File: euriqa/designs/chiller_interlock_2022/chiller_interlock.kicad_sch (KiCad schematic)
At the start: 0 parts

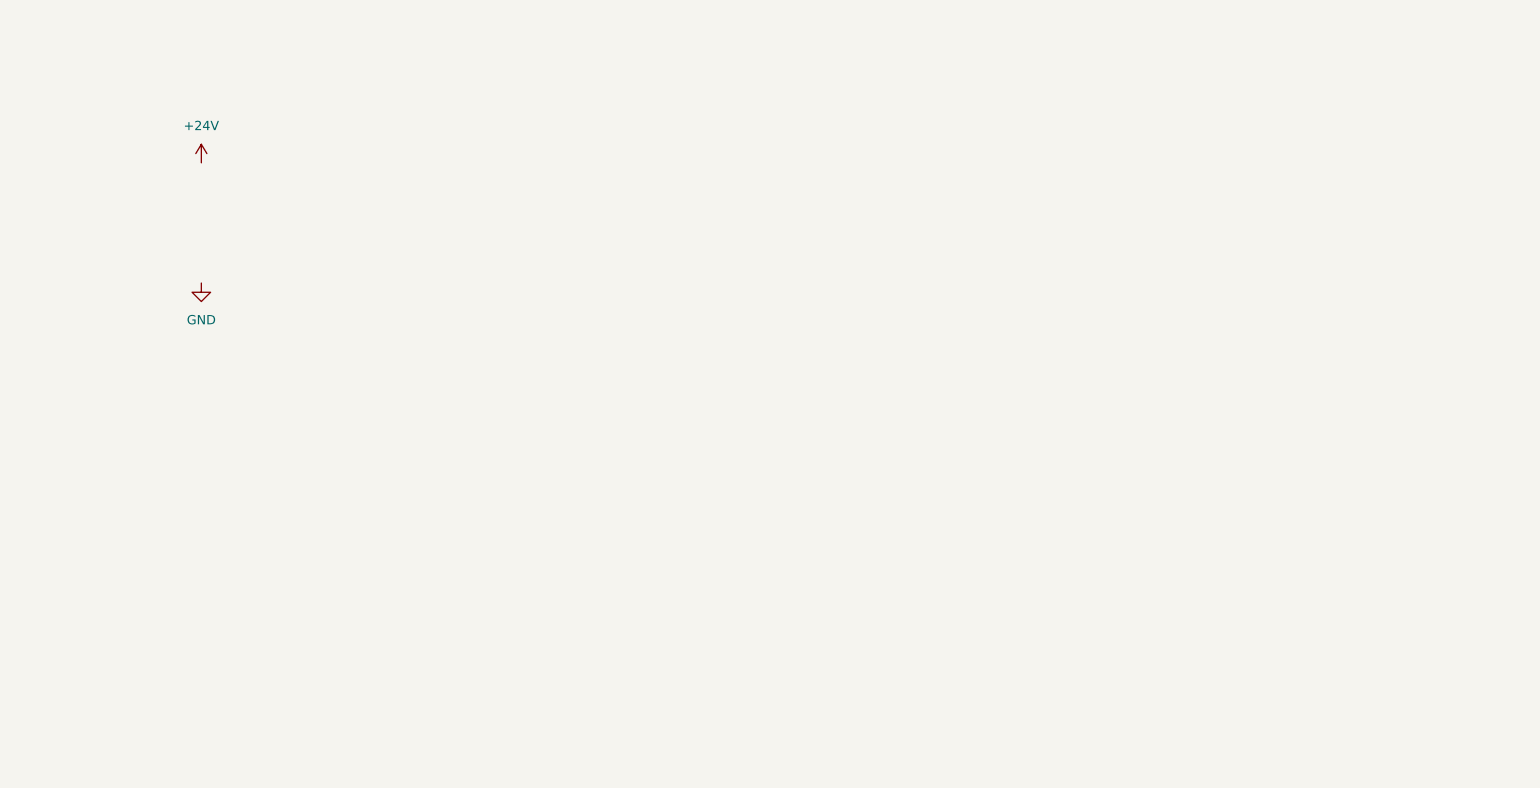
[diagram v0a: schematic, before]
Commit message: [euriqa/design/chiller_interlock_2022] Schematics
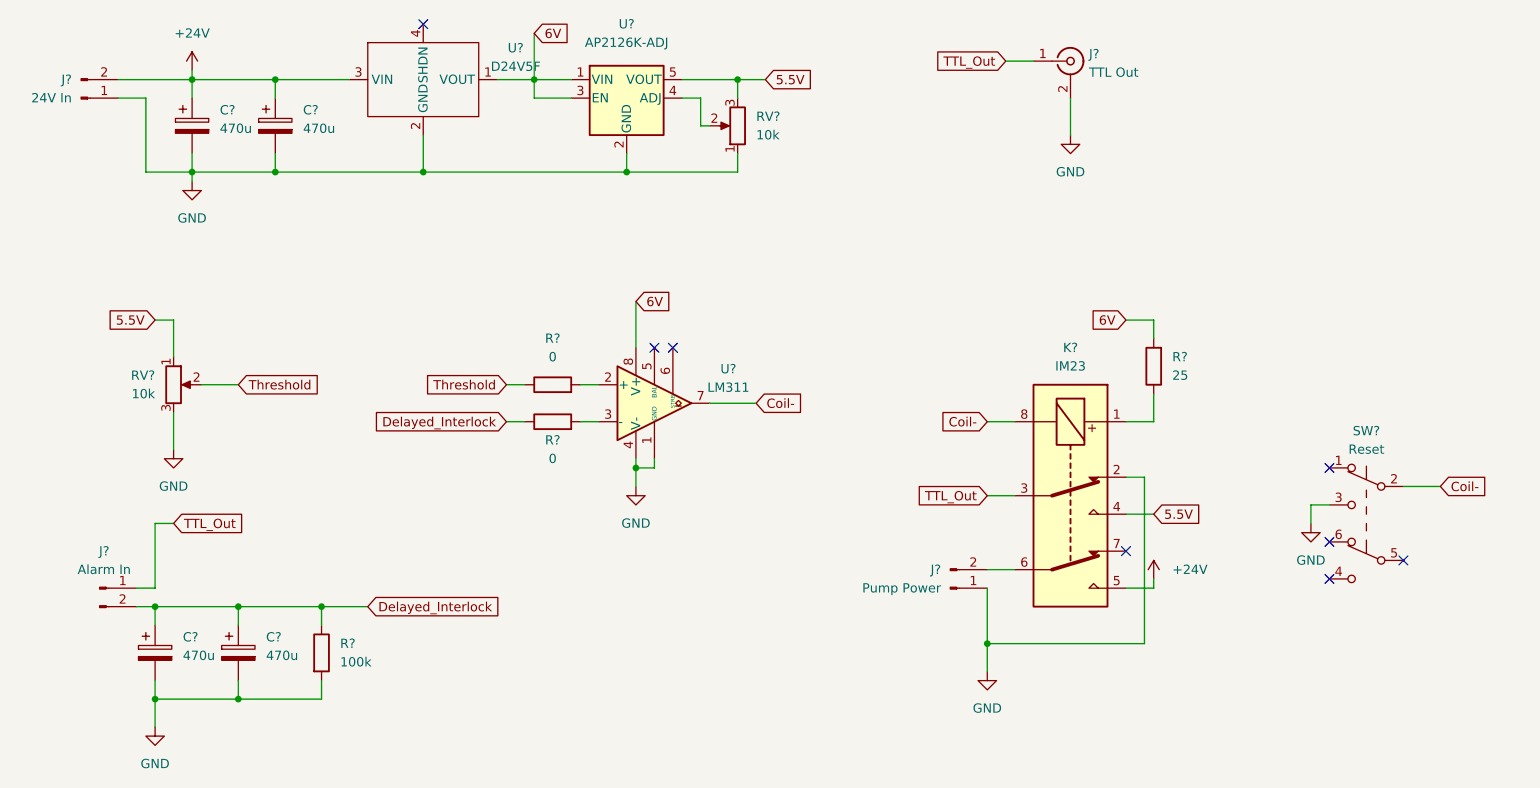
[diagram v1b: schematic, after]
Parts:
- added C? (x4): 470u, symbol Device:C_Polarized
- added J?: Alarm In, symbol Connector:Conn_01x02_Male
- added J?: Pump Power, symbol Connector:Conn_01x02_Male
- added J?: 24V In, symbol Connector:Conn_01x02_Male
- added J?: TTL Out, symbol Connector:Conn_Coaxial
- added K?: IM23, symbol Relay:IM23
- added R? (x2): 0, symbol Device:R
- added R?: 100k, symbol Device:R
- added R?: 25, symbol Device:R
- added RV? (x2): 10k, symbol Device:R_Potentiometer
- added SW?: Reset, symbol Switch2:SW_Push_DPDT2
- added U?: LM311, symbol Comparator:LM311
- added U?: AP2126K-ADJ, Package_TO_SOT_SMD:SOT-23-5, symbol regulator:AP2126K-ADJ
- added U?: D24V5F, symbol regulator:D24V5F
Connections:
- net +24V: now also C?.1, C?.1, J?.2 (Pin_2), K?.5, U?.3 (VIN)
- net GND: now also C?.2, C?.2, C?.2, C?.2, J?.1 (Pin_1), J?.1 (Pin_1), J?.2 (Ext), K?.2, R?.2, RV?.1, RV?.3, SW?.3 (C), U?.1 (GND), U?.2 (GND), U?.2 (GND), U?.4 (V-)
- new net: R?.2, U?.2 (+)
- new net: R?.2, U?.3 (-)
- new net: K?.1, R?.1
- new net: J?.2 (Pin_2), K?.6
- new net: RV?.2, U?.4 (ADJ)
- new net 5.5V: K?.4, RV?.1, RV?.3, U?.5 (VOUT)
- new net 6V: R?.2, U?.1 (VIN), U?.1 (VOUT), U?.3 (EN), U?.8 (V+)
- new net Coil-: K?.8, SW?.2 (B), U?.7
- new net Delayed_Interlock: C?.1, C?.1, J?.2 (Pin_2), R?.1, R?.1
- new net TTL_Out: J?.1 (In), J?.1 (Pin_1), K?.3
- new net Threshold: R?.1, RV?.2
- no-connect marks 0 -> 8

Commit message: [euriqa/design/chiller_interlock_2022] Consistent connector pin order, footprint assignment
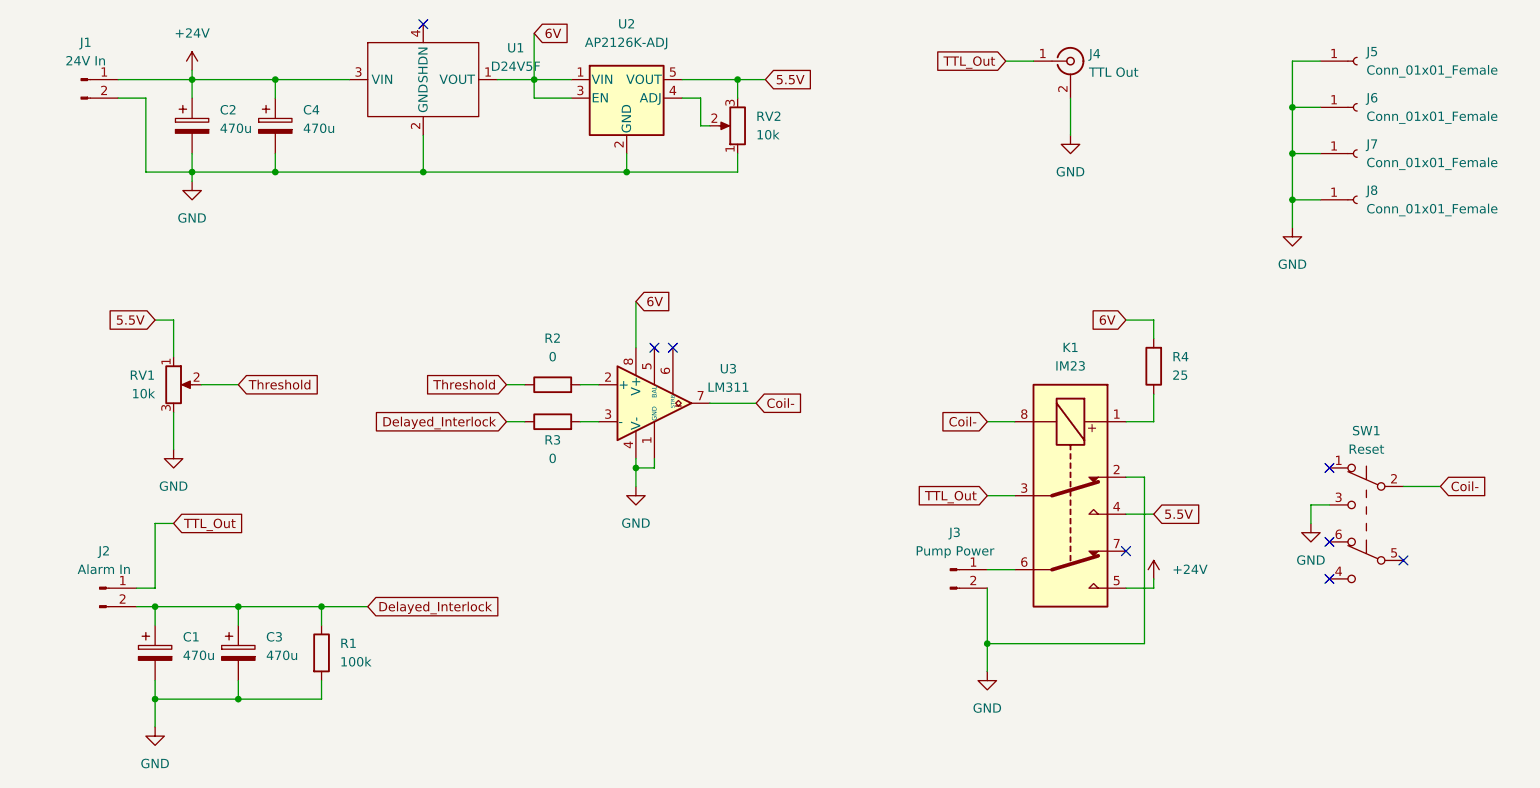
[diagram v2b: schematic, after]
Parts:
- added J5, J6, J7, J8: Conn_01x01_Female, MountingHole:MountingHole_3.7mm_Pad, symbol Connector:Conn_01x01_Female
- C1, C2, C3, C4: renamed from C?; footprint (none) -> Capacitor_THT:CP_Radial_D10.0mm_P3.50mm
- J1, J2, J3: renamed from J?; footprint (none) -> Connector_Phoenix_MC:PhoenixContact_MCV_1,5_2-G-3.5_1x02_P3.50mm_Vertical
- J4: renamed from J?; footprint (none) -> Connector_Coaxial:BNC_Amphenol_B6252HB-NPP3G-50_Horizontal
- K1: renamed from K?; footprint (none) -> Relay_THT:Relay_DPDT_AXICOM_IMSeries_Pitch5.08mm
- R1, R2, R3, R4: renamed from R?; footprint (none) -> Resistor_THT:R_Axial_DIN0207_L6.3mm_D2.5mm_P10.16mm_Horizontal
- RV1, RV2: renamed from RV?; footprint (none) -> Potentiometer_SMD:Potentiometer_Bourns_3214W_Vertical
- SW1: renamed from SW?; footprint (none) -> Button_Switch2:E-Switch_TL2233
- U1: renamed from U?; footprint (none) -> Regulator2:D24V5F
- U3: renamed from U?; footprint (none) -> Package_SO:SOIC-8_3.9x4.9mm_P1.27mm
- gave numbers to parts that had none: 1
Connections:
- net +24V: now also J1.1 (Pin_1); no longer J1.2 (Pin_2)
- net GND: now also J1.2 (Pin_2), J3.2 (Pin_2), J5.1 (Pin_1), J6.1 (Pin_1), J7.1 (Pin_1), J8.1 (Pin_1); no longer J1.1 (Pin_1), J3.1 (Pin_1)
- net at K1.6: now also J3.1 (Pin_1); no longer J3.2 (Pin_2)

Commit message: [euriqa/design/chiller_interlock_2022] Layout and routing
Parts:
- removed J8: Conn_01x01_Female, MountingHole:MountingHole_3.7mm_Pad, symbol Connector:Conn_01x01_Female
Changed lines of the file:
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@@
   (junction (at 35.56 97.79) (diameter 0) (color 0 0 0 0)
   )
-  (junction (at 191.77 41.91) (diameter 0) (color 0 0 0 0)
-  )
   (junction (at 46.99 97.79) (diameter 0) (color 0 0 0 0)
   )
@@
   (junction (at 101.6 78.74) (diameter 0) (color 0 0 0 0)
   )
+  (junction (at 35.56 110.49) (diameter 0) (color 0 0 0 0)
+  )
+  (junction (at 72.39 38.1) (diameter 0) (color 0 0 0 0)
+  )
+  (junction (at 40.64 38.1) (diameter 0) (color 0 0 0 0)
+  )
+  (junction (at 100.33 38.1) (diameter 0) (color 0 0 0 0)
+  )
+  (junction (at 40.64 25.4) (diameter 0) (color 0 0 0 0)
+  )
+  (junction (at 191.77 29.21) (diameter 0) (color 0 0 0 0)
+  )
+  (junction (at 46.99 110.49) (diameter 0) (color 0 0 0 0)
+  )
+  (junction (at 149.86 102.87) (diameter 0) (color 0 0 0 0)
+  )
   (junction (at 191.77 35.56) (diameter 0) (color 0 0 0 0)
-  )
-  (junction (at 35.56 110.49) (diameter 0) (color 0 0 0 0)
-  )
-  (junction (at 72.39 38.1) (diameter 0) (color 0 0 0 0)
-  )
-  (junction (at 40.64 38.1) (diameter 0) (color 0 0 0 0)
-  )
-  (junction (at 100.33 38.1) (diameter 0) (color 0 0 0 0)
-  )
-  (junction (at 40.64 25.4) (diameter 0) (color 0 0 0 0)
-  )
-  (junction (at 191.77 29.21) (diameter 0) (color 0 0 0 0)
-  )
-  (junction (at 46.99 110.49) (diameter 0) (color 0 0 0 0)
-  )
-  (junction (at 149.86 102.87) (diameter 0) (color 0 0 0 0)
   )
   (junction (at 87.63 25.4) (diameter 0) (color 0 0 0 0)
@@
     (stroke (width 0) (type default) (color 0 0 0 0))
   )
-  (wire (pts (xy 191.77 45.72) (xy 191.77 41.91))
-    (stroke (width 0) (type default) (color 0 0 0 0))
-  )
   (wire (pts (xy 101.6 78.74) (xy 101.6 81.28))
     (stroke (width 0) (type default) (color 0 0 0 0))
@@
     (stroke (width 0) (type default) (color 0 0 0 0))
   )
+  (wire (pts (xy 191.77 35.56) (xy 191.77 41.91))
+    (stroke (width 0) (type default) (color 0 0 0 0))
+  )
   (wire (pts (xy 168.91 58.42) (xy 172.72 58.42))
     (stroke (width 0) (type default) (color 0 0 0 0))
@@
     (stroke (width 0) (type default) (color 0 0 0 0))
   )
-  (wire (pts (xy 191.77 41.91) (xy 195.58 41.91))
-    (stroke (width 0) (type default) (color 0 0 0 0))
-  )
   (wire (pts (xy 34.29 27.94) (xy 34.29 38.1))
     (stroke (width 0) (type default) (color 0 0 0 0))
@@
   )
   (wire (pts (xy 83.82 72.39) (xy 86.36 72.39))
-    (stroke (width 0) (type default) (color 0 0 0 0))
-  )
-  (wire (pts (xy 191.77 41.91) (xy 191.77 35.56))
     (stroke (width 0) (type default) (color 0 0 0 0))
   )
@@
     (pin "1")
     (pin "2")
-  )
-  (symbol (lib_id "Connector:Conn_01x01_Female") (at 200.66 41.91 0) (unit 1)
-    (in_bom yes) (on_board yes) (fields_autoplaced)
-    (property "Reference" "J8" (id 0) (at 201.93 40.6399 0)
-      (effects (font (size 1.27 1.27)) (justify left))
-    )
-    (property "Value" "Conn_01x01_Female" (id 1) (at 201.93 43.1799 0)
-      (effects (font (size 1.27 1.27)) (justify left))
-    )
-    (property "Footprint" "MountingHole:MountingHole_3.7mm_Pad" (id 2) (at 200.66 41.91 0)
-      (effects (font (size 1.27 1.27)) hide)
-    )
-    (property "Datasheet" "~" (id 3) (at 200.66 41.91 0)
-      (effects (font (size 1.27 1.27)) hide)
-    )
-    (pin "1")
   )
   (symbol (lib_id "power:GND") (at 161.29 33.02 0) (unit 1)
@@
     (pin "1")
   )
-  (symbol (lib_id "power:GND") (at 191.77 45.72 0) (unit 1)
-    (in_bom yes) (on_board yes) (fields_autoplaced)
-    (property "Reference" "#PWR010" (id 0) (at 191.77 52.07 0)
-      (effects (font (size 1.27 1.27)) hide)
-    )
-    (property "Value" "GND" (id 1) (at 191.77 50.8 0))
-    (property "Footprint" "" (id 2) (at 191.77 45.72 0)
-      (effects (font (size 1.27 1.27)) hide)
-    )
-    (property "Datasheet" "" (id 3) (at 191.77 45.72 0)
+  (symbol (lib_id "power:GND") (at 191.77 41.91 0) (unit 1)
+    (in_bom yes) (on_board yes) (fields_autoplaced)
+    (property "Reference" "#PWR010" (id 0) (at 191.77 48.26 0)
+      (effects (font (size 1.27 1.27)) hide)
+    )
+    (property "Value" "GND" (id 1) (at 191.77 46.99 0))
+    (property "Footprint" "" (id 2) (at 191.77 41.91 0)
+      (effects (font (size 1.27 1.27)) hide)
+    )
+    (property "Datasheet" "" (id 3) (at 191.77 41.91 0)
       (effects (font (size 1.27 1.27)) hide)
     )
@@
       (reference "J7") (unit 1) (value "Conn_01x01_Female") (footprint "MountingHole:MountingHole_3.7mm_Pad")
     )
-    (path "/39b819d8-dc93-40ea-a3fb-73b16c8f8f00"
-      (reference "J8") (unit 1) (value "Conn_01x01_Female") (footprint "MountingHole:MountingHole_3.7mm_Pad")
-    )
     (path "/50de0bbb-8576-427b-8ac6-2651ca27714a"
